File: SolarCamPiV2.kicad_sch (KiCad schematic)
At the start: 86 parts, among them Q2 AO3401A, Q3 2N7002, Q4 AO3401A, Q5 2N7002, Q6 BSS84, U1 CN3767, U2 HT7533, U3 SY8113B

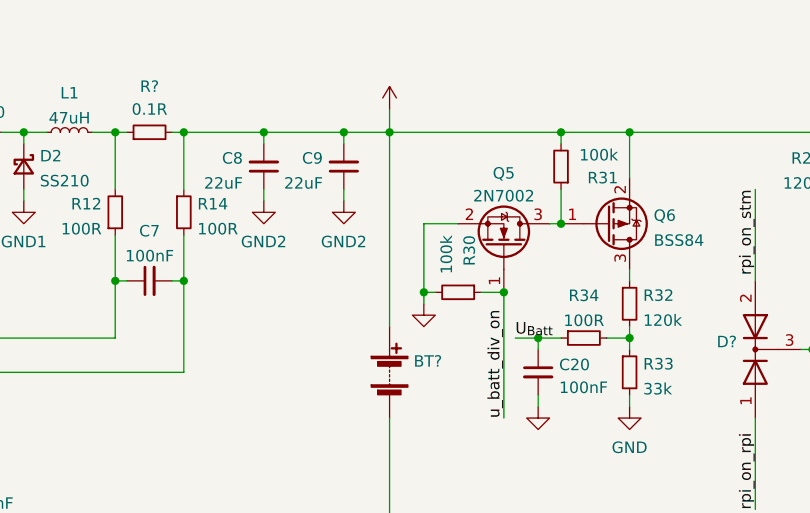
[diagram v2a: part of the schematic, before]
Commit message: Add battery fuse
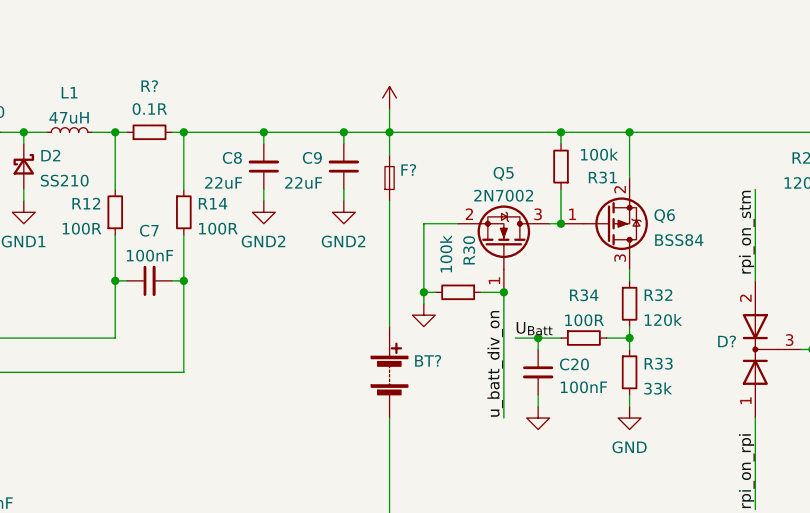
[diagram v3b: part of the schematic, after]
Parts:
- added F?: (no value), symbol Device:Fuse_Small
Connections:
- net +BATT: now also F?.2; no longer BT?.1 (+)
- new net: BT?.1 (+), F?.1
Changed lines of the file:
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@@
     (stroke (width 0) (type default) (color 0 0 0 0))
   )
+  (wire (pts (xy 140.97 27.94) (xy 140.97 30.48))
+    (stroke (width 0) (type default) (color 0 0 0 0))
+  )
   (wire (pts (xy 203.2 156.21) (xy 203.2 154.94))
     (stroke (width 0) (type default) (color 0 0 0 0))
@@
     (stroke (width 0) (type default) (color 0 0 0 0))
   )
-  (wire (pts (xy 140.97 27.94) (xy 140.97 49.53))
-    (stroke (width 0) (type default) (color 0 0 0 0))
-  )
   (wire (pts (xy 218.44 106.68) (xy 218.44 109.22))
     (stroke (width 0) (type default) (color 0 0 0 0))
@@
     (stroke (width 0) (type default) (color 0 0 0 0))
   )
+  (wire (pts (xy 140.97 35.56) (xy 140.97 49.53))
+    (stroke (width 0) (type default) (color 0 0 0 0))
+  )
   (wire (pts (xy 135.89 27.94) (xy 140.97 27.94))
     (stroke (width 0) (type default) (color 0 0 0 0))
@@
     (pin "1")
   )
+  (symbol (lib_id "Device:Fuse_Small") (at 140.97 33.02 90) (unit 1)
+    (in_bom yes) (on_board yes) (fields_autoplaced)
+    (property "Reference" "F?" (id 0) (at 142.113 32.1853 90)
+      (effects (font (size 1.27 1.27)) (justify right))
+    )
+    (property "Value" "" (id 1) (at 142.113 34.7222 90)
+      (effects (font (size 1.27 1.27)) (justify right))
+    )
+    (property "Footprint" "" (id 2) (at 140.97 33.02 0)
+      (effects (font (size 1.27 1.27)) hide)
+    )
+    (property "Datasheet" "~" (id 3) (at 140.97 33.02 0)
+      (effects (font (size 1.27 1.27)) hide)
+    )
+    (property "LCSC" "C354895" (id 4) (at 140.97 33.02 0)
+      (effects (font (size 1.27 1.27)) hide)
+    )
+    (pin "1")
+    (pin "2")
+  )
   (symbol (lib_id "power:GND") (at 22.86 44.45 0) (unit 1)
     (in_bom yes) (on_board yes) (fields_autoplaced)
@@
       (reference "D?") (unit 1) (value "PWR") (footprint "LED_SMD:LED_0603_1608Metric")
     )
+    (path "/d601264f-35e5-4f9b-a393-f83a16e7d4e0"
+      (reference "F?") (unit 1) (value "2A") (footprint "Fuse:Fuse_1206_3216Metric")
+    )
     (path "/819a8413-6af3-4f54-a057-6464065995fe"

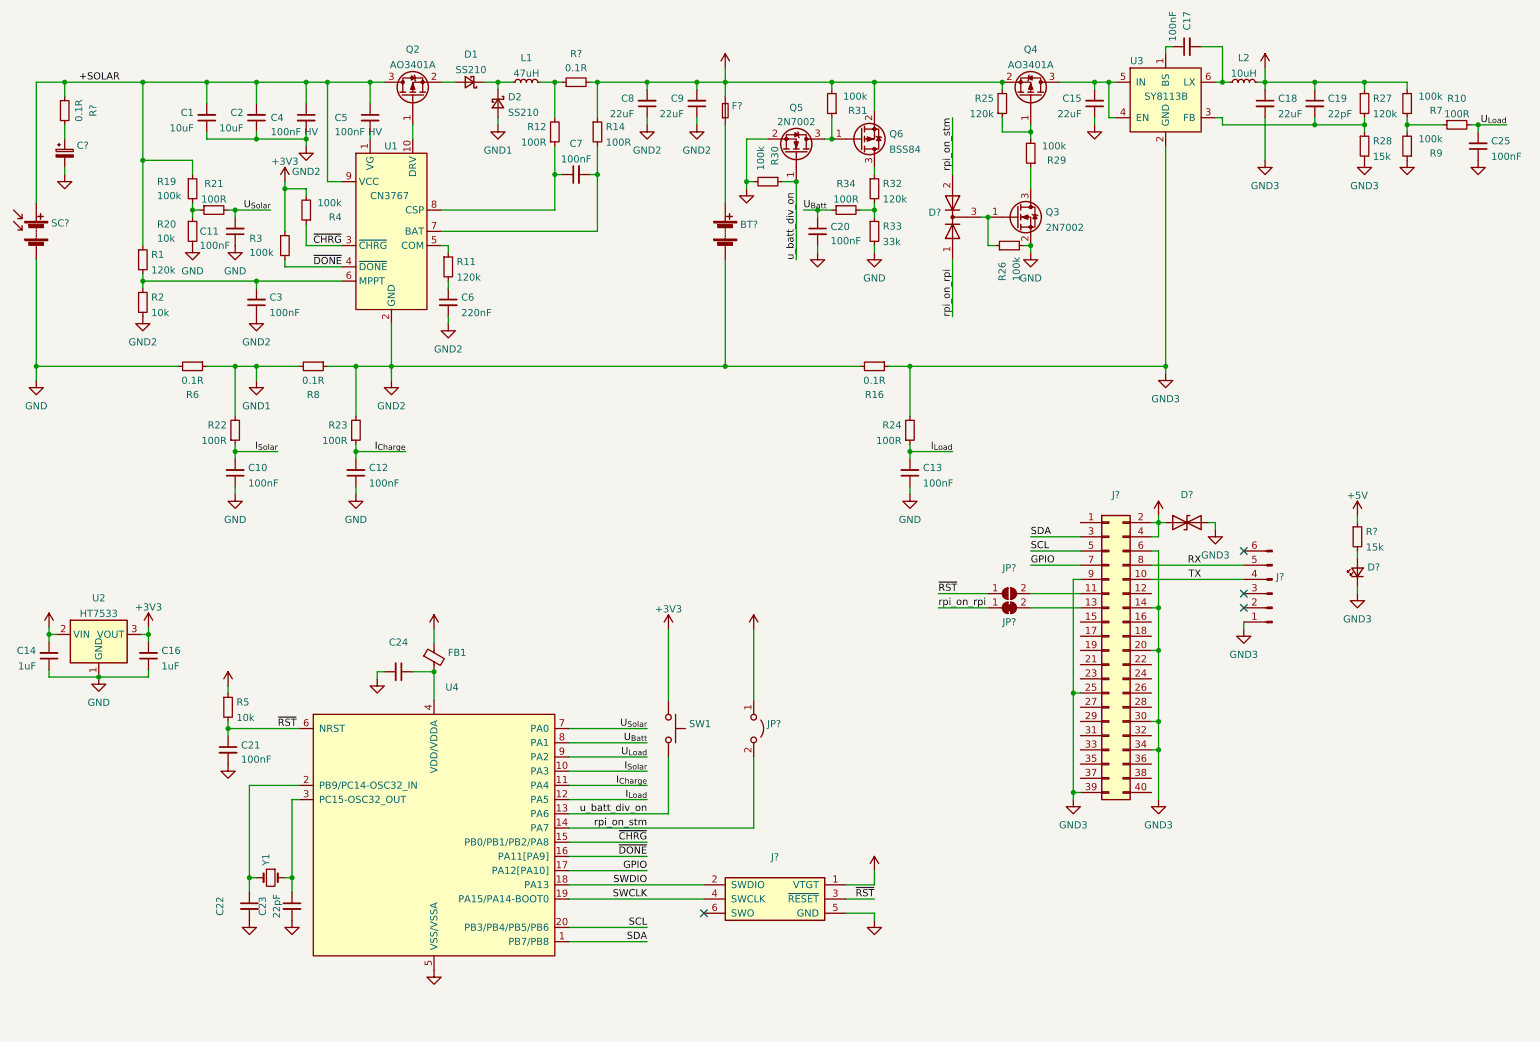
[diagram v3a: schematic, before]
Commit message: Add reverse polarity protection
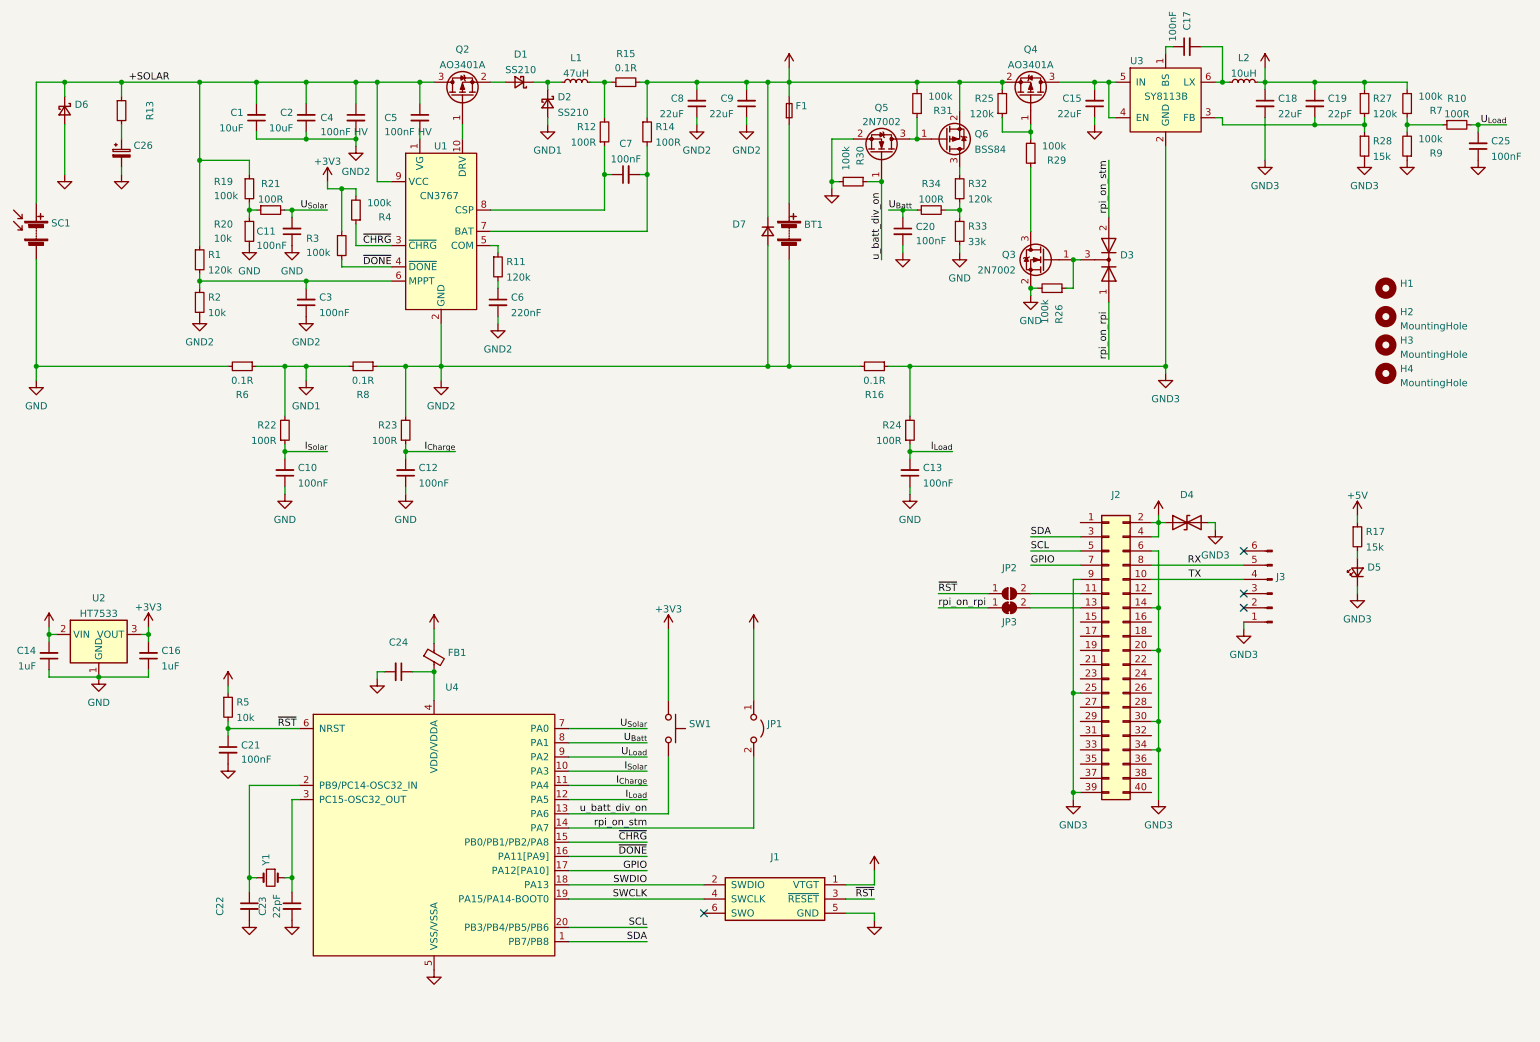
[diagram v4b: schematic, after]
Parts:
- added D6: (no value), symbol Device:D_Schottky_Small
- added D7: (no value), symbol Device:D_Small
- added H1: (no value), symbol Mechanical:MountingHole
- added H2, H3, H4: MountingHole, MountingHole:MountingHole_2.7mm_M2.5, symbol Mechanical:MountingHole
- BT1: renamed from BT?; LCSC (none) -> C474892
- R13: renamed from R?; value 0.1R -> (none); footprint Resistor_SMD:R_1206_3216Metric -> (none); LCSC C25334 -> C17928
- SC1: renamed from SC?; LCSC (none) -> C474892
- gave numbers to parts that had none: 13
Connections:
- net +BATT: now also D7.1 (K)
- net +SOLAR: now also D6.1 (K)
- net GND: now also D6.2 (A)
- net GND2: now also D7.2 (A)
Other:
- moved on the sheet: BT1, C1, C10, C11, C12, C2, C20, C26, C3, C4, C5, C6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

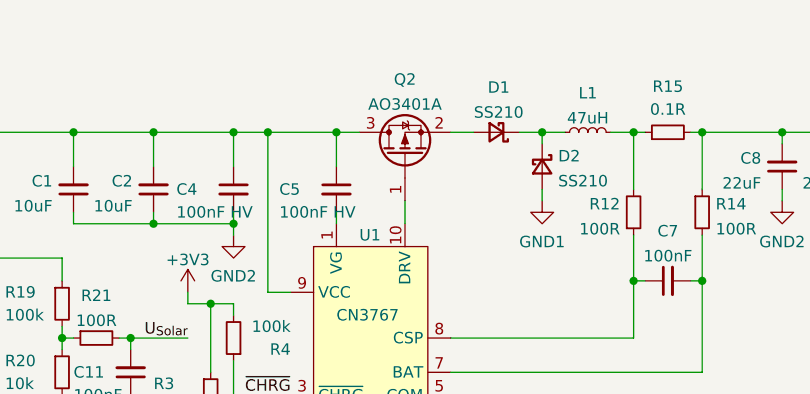
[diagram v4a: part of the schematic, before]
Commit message: Fix Q2 polarity
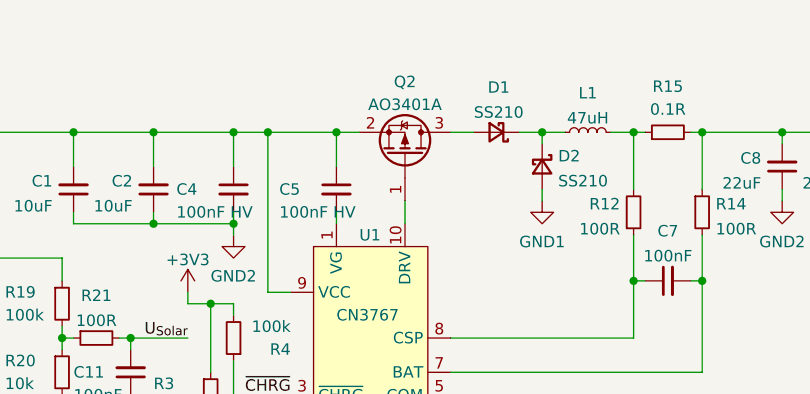
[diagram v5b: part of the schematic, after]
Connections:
- net +SOLAR: now also Q2.2 (S); no longer Q2.3 (D)
- net at D1.2 (A): now also Q2.3 (D); no longer Q2.2 (S)
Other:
- moved on the sheet: Q2
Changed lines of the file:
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@@
     (pin "9")
   )
-  (symbol (lib_id "Transistor_FET:AO3401A") (at 93.98 30.48 90) (unit 1)
+  (symbol (lib_id "Transistor_FET:AO3401A") (at 93.98 30.48 270) (mirror x) (unit 1)
     (in_bom yes) (on_board yes) (fields_autoplaced)
-    (property "Reference" "Q2" (id 0) (at 93.98 22.0685 90))
-    (property "Value" "AO3401A" (id 1) (at 93.98 24.8436 90))
-    (property "Footprint" "Package_TO_SOT_SMD:SOT-23" (id 2) (at 95.885 25.4 0)
+    (property "Reference" "Q2" (id 0) (at 93.98 22.3352 90))
+    (property "Value" "AO3401A" (id 1) (at 93.98 24.8721 90))
+    (property "Footprint" "Package_TO_SOT_SMD:SOT-23" (id 2) (at 92.075 25.4 0)
       (effects (font (size 1.27 1.27) italic) (justify left) hide)
     )

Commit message: Layout power conversion subcomponents
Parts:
- added Q1: AO3401A, Package_TO_SOT_SMD:SOT-23, symbol Transistor_FET:AO3401A
- BT1: value (none) -> Battery; footprint (none) -> TerminalBlock_4Ucon:TerminalBlock_4Ucon_1x02_P3.50mm_Horizontal
- C22: value (none) -> 22pF; footprint (none) -> Capacitor_SMD:C_0402_1005Metric
- C24: value (none) -> 1uF; footprint (none) -> Capacitor_SMD:C_0402_1005Metric
- C26: value (none) -> 220uF 35V; footprint (none) -> Capacitor_SMD:CP_Elec_10x10
- D3: value (none) -> BAV70; footprint (none) -> Package_TO_SOT_SMD:SOT-23
- D4: value (none) -> 6.8CA; footprint (none) -> Diode_SMD:D_SMB
- D5: value (none) -> PWR; footprint (none) -> LED_SMD:LED_0603_1608Metric
- D6: value (none) -> SS36; footprint (none) -> Diode_SMD:D_SMC
- D7: value (none) -> M7; footprint (none) -> Diode_SMD:D_SMA
- F1: value (none) -> 2A; footprint (none) -> Fuse:Fuse_1206_3216Metric
- FB1: value (none) -> 100R@100MHz; footprint (none) -> Inductor_SMD:L_0805_2012Metric
- H1: value (none) -> MountingHole; footprint (none) -> MountingHole:MountingHole_2.7mm_M2.5
- J1: value (none) -> TagConnect_TC2030_SWD; footprint (none) -> Connector:Tag-Connect_TC2030-IDC-NL_2x03_P1.27mm_Vertical
- J2: value (none) -> RPi; footprint (none) -> Connector_PinSocket_2.54mm:PinSocket_2x20_P2.54mm_Vertical
- J3: value (none) -> FTDI_RPI; footprint (none) -> Connector_PinHeader_2.54mm:PinHeader_1x06_P2.54mm_Vertical
- JP1: value (none) -> Force on; footprint (none) -> Connector_PinHeader_2.54mm:PinHeader_1x02_P2.54mm_Horizontal
- JP2: value (none) -> Pi -> STM RST; footprint (none) -> Jumper:SolderJumper-2_P1.3mm_Open_Pad1.0x1.5mm
- JP3: value (none) -> Pi -> PWR ON; footprint (none) -> Jumper:SolderJumper-2_P1.3mm_Bridged_Pad1.0x1.5mm
- R13: value (none) -> 1R; footprint (none) -> Resistor_SMD:R_1206_3216Metric
- SC1: value (none) -> Solar_Cells; footprint (none) -> TerminalBlock_4Ucon:TerminalBlock_4Ucon_1x02_P3.50mm_Horizontal
- SW1: value (none) -> User
- U4: value (none) -> STM32G031Fx; footprint (none) -> Package_SO:TSSOP-20_4.4x6.5mm_P0.65mm
- Y1: value (none) -> 32.768kHz; footprint (none) -> Crystal:Crystal_SMD_3215-2Pin_3.2x1.5mm
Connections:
- net +SOLAR: now also Q1.2 (S)
- net at Q2.1 (G), U1.10 (DRV): now also Q1.1 (G)
- net at D1.2 (A), Q2.3 (D): now also Q1.3 (D)
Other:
- moved on the sheet: BT1, C1, C10, C11, C12, C13, C14, C15, C16, C17, C18, C19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
